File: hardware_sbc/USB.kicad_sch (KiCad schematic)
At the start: 31 parts, among them J13 USB_C_Receptacle, U1B IMX8MM, U8 NX20P3483UK, U9 PTN5110NHQZ

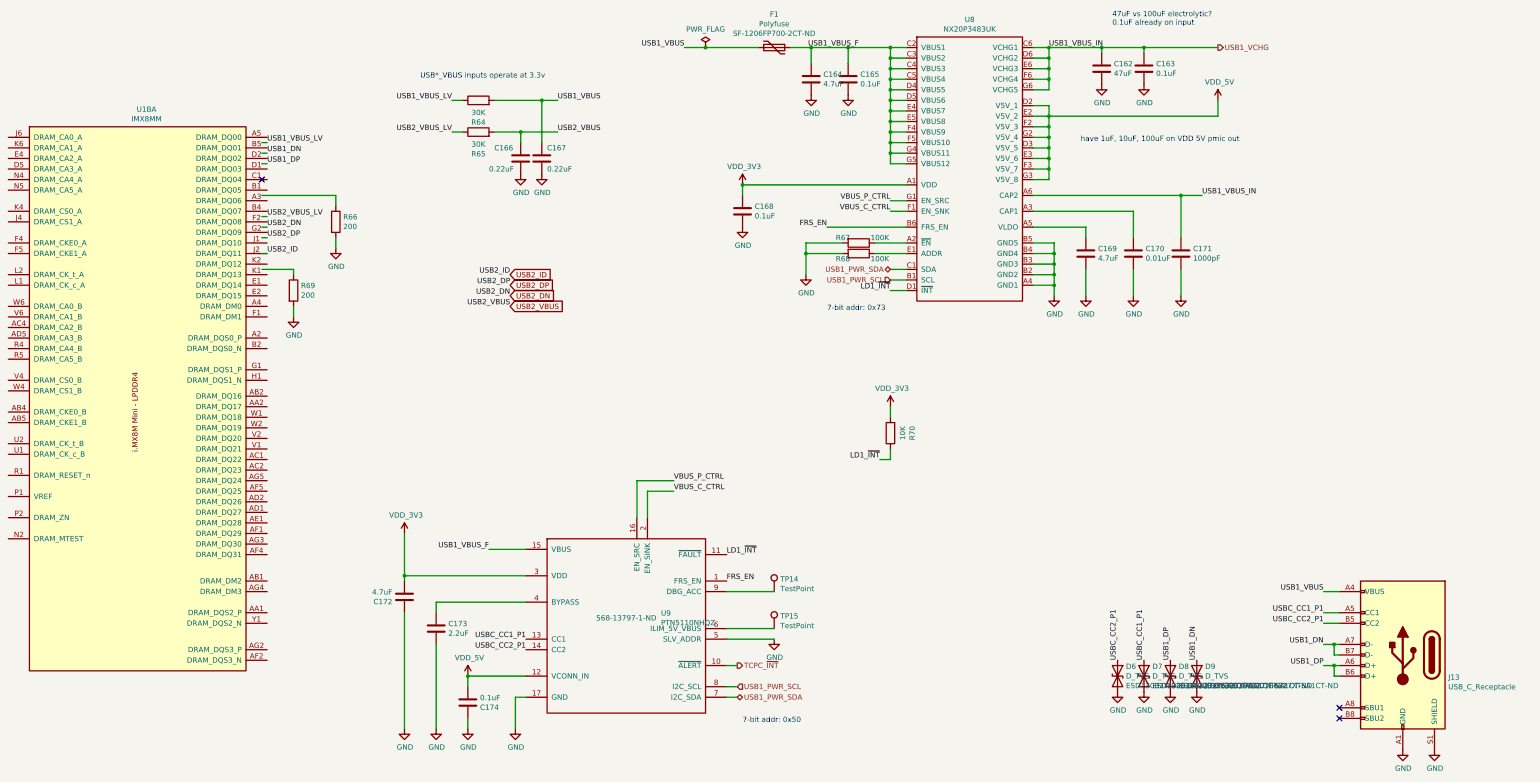
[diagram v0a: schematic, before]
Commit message: Updated production files and fixed schematic link issue.
Fixed schematic unit number issue and re-linked to PCB.
New gerbers, STEP file, schematic PDF.
Deleted old KiCAD 6 files.
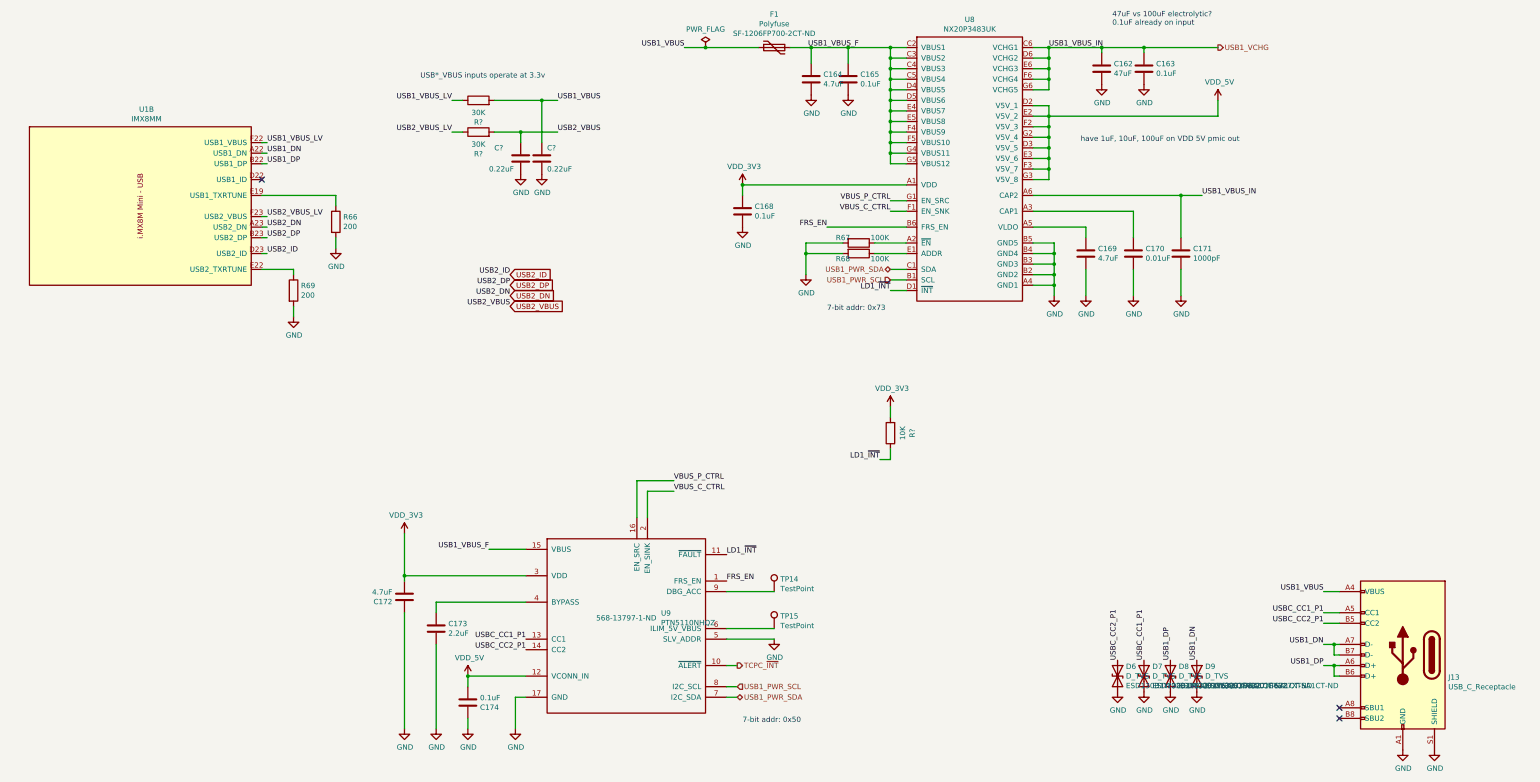
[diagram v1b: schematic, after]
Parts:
- renumbered C166 to C?, C167 to C?, R64 to R?, R65 to R?, R70 to R?, U1B to U1
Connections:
- net USB1_DN: now also U1.A22 (USB1_DN)
- net USB1_DP: now also U1.B22 (USB1_DP)
- net USB1_VBUS_LV: now also U1.F22 (USB1_VBUS)
- net USB2_DN: now also U1.A23 (USB2_DN)
- net USB2_DP: now also U1.B23 (USB2_DP)
- net USB2_ID: now also U1.D23 (USB2_ID); no longer U1.J2 (DRAM_DQ11)
- net USB2_VBUS_LV: now also U1.F23 (USB2_VBUS)
- net at R69.1: now also U1.E22 (USB2_TXRTUNE)
- net at R66.1: now also U1.E19 (USB1_TXRTUNE)
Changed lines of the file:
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@@
 	(label "USB1_DN"
 		(at 96.52 72.39 0)
+		(fields_autoplaced yes)
 		(effects
 			(font
@@
 	(label "VBUS_C_CTRL"
 		(at 246.38 86.36 180)
+		(fields_autoplaced yes)
 		(effects
 			(font
@@
 	(label "USB2_ID"
 		(at 96.52 96.52 0)
+		(fields_autoplaced yes)
 		(effects
 			(font
@@
 	(label "FRS_EN"
 		(at 207.01 175.26 0)
+		(fields_autoplaced yes)
 		(effects
 			(font
@@
 	(label "USBC_CC2_P1"
 		(at 300.99 194.31 90)
+		(fields_autoplaced yes)
 		(effects
 			(font
@@
 	(label "USBC_CC1_P1"
 		(at 350.52 182.88 180)
+		(fields_autoplaced yes)
 		(effects
 			(font
@@
 	(label "USB1_VBUS_IN"
 		(at 321.31 82.55 0)
+		(fields_autoplaced yes)
 		(effects
 			(font
@@
 	(label "VBUS_C_CTRL"
 		(at 194.31 153.67 0)
+		(fields_autoplaced yes)
 		(effects
 			(font
@@
 	(label "LD1_~{INT}"
 		(at 207.01 168.91 0)
+		(fields_autoplaced yes)
 		(effects
 			(font
@@
 	(label "USB2_VBUS_LV"
 		(at 140.97 67.31 180)
+		(fields_autoplaced yes)
 		(effects
 			(font
@@
 	(label "USBC_CC1_P1"
 		(at 158.75 189.23 180)
+		(fields_autoplaced yes)
 		(effects
 			(font
@@
 	(label "USB1_VBUS_F"
 		(at 149.86 167.64 180)
+		(fields_autoplaced yes)
 		(effects
 			(font
@@
 	(label "USB1_VBUS"
 		(at 196.85 46.99 180)
+		(fields_autoplaced yes)
 		(effects
 			(font
@@
 	(label "USB1_DN"
 		(at 320.04 194.31 90)
+		(fields_autoplaced yes)
 		(effects
 			(font
@@
 	(label "LD1_~{INT}"
 		(at 243.84 146.05 180)
+		(fields_autoplaced yes)
 		(effects
 			(font
@@
 	(label "VBUS_P_CTRL"
 		(at 194.31 151.13 0)
+		(fields_autoplaced yes)
 		(effects
 			(font
@@
 	(label "USB1_DP"
 		(at 313.69 194.31 90)
+		(fields_autoplaced yes)
 		(effects
 			(font
@@
 	(label "USB1_VBUS_IN"
 		(at 284.48 46.99 0)
+		(fields_autoplaced yes)
 		(effects
 			(font
@@
 	(label "USB1_VBUS"
 		(at 350.52 177.8 180)
+		(fields_autoplaced yes)
 		(effects
 			(font
@@
 	(label "USB1_VBUS"
 		(at 166.37 59.69 0)
+		(fields_autoplaced yes)
 		(effects
 			(font
@@
 	(label "USBC_CC2_P1"
 		(at 158.75 191.77 180)
+		(fields_autoplaced yes)
 		(effects
 			(font
@@
 	(label "USB2_DP"
 		(at 154.94 104.14 180)
+		(fields_autoplaced yes)
 		(effects
 			(font
@@
 	(label "USBC_CC1_P1"
 		(at 307.34 194.31 90)
+		(fields_autoplaced yes)
 		(effects
 			(font
@@
 	(label "USB2_ID"
 		(at 154.94 101.6 180)
+		(fields_autoplaced yes)
 		(effects
 			(font
@@
 	(label "USB1_VBUS_LV"
 		(at 96.52 69.85 0)
+		(fields_autoplaced yes)
 		(effects
 			(font
@@
 	(label "USB1_VBUS_F"
 		(at 238.76 46.99 180)
+		(fields_autoplaced yes)
 		(effects
 			(font
@@
 	(label "USBC_CC2_P1"
 		(at 350.52 185.42 180)
+		(fields_autoplaced yes)
 		(effects
 			(font
@@
 	(label "VBUS_P_CTRL"
 		(at 246.38 83.82 180)
+		(fields_autoplaced yes)
 		(effects
 			(font
@@
 	(label "USB2_VBUS"
 		(at 154.94 109.22 180)
+		(fields_autoplaced yes)
 		(effects
 			(font
@@
 	(label "USB1_DP"
 		(at 350.52 195.58 180)
+		(fields_autoplaced yes)
 		(effects
 			(font
@@
 	(label "USB2_VBUS"
 		(at 166.37 67.31 0)
+		(fields_autoplaced yes)
 		(effects
 			(font
@@
 	(label "USB1_DN"
 		(at 350.52 190.5 180)
+		(fields_autoplaced yes)
 		(effects
 			(font
@@
 	(label "LD1_~{INT}"
 		(at 246.38 105.41 180)
+		(fields_autoplaced yes)
 		(effects
 			(font
@@
 	(label "USB2_DN"
 		(at 96.52 90.17 0)
+		(fields_autoplaced yes)
 		(effects
 			(font
@@
 	(label "USB1_DP"
 		(at 96.52 74.93 0)
+		(fields_autoplaced yes)
 		(effects
 			(font
@@
 	(label "USB2_DN"
 		(at 154.94 106.68 180)
+		(fields_autoplaced yes)
 		(effects
 			(font
@@
 	(label "FRS_EN"
 		(at 231.14 90.17 180)
+		(fields_autoplaced yes)
 		(effects
 			(font
@@
 	(label "USB1_VBUS_LV"
 		(at 140.97 59.69 180)
+		(fields_autoplaced yes)
 		(effects
 			(font
@@
 	(label "USB2_DP"
 		(at 96.52 92.71 0)
+		(fields_autoplaced yes)
 		(effects
 			(font
@@
 	(label "USB2_VBUS_LV"
 		(at 96.52 87.63 0)
+		(fields_autoplaced yes)
 		(effects
 			(font
@@
 		(shape output)
 		(at 325.12 46.99 0)
+		(fields_autoplaced yes)
 		(effects
 			(font
@@
 		(shape bidirectional)
 		(at 246.38 100.33 180)
+		(fields_autoplaced yes)
 		(effects
 			(font
@@
 		(shape input)
 		(at 246.38 102.87 180)
+		(fields_autoplaced yes)
 		(effects
 			(font
@@
 		(shape bidirectional)
 		(at 209.55 203.2 0)
+		(fields_autoplaced yes)
 		(effects
 			(font
@@
 		(shape input)
 		(at 209.55 200.66 0)
+		(fields_autoplaced yes)
 		(effects
 			(font
@@
 		(shape output)
 		(at 209.55 195.58 0)
+		(fields_autoplaced yes)
 		(effects
 			(font
@@
 		(lib_id "mxenc:MIMX8MM6DVTLZAA")
 		(at 66.04 134.62 0)
-		(unit 1)
+		(unit 2)
 		(exclude_from_sim no)
 		(in_bom yes)
 		(on_board yes)
 		(dnp no)
-		(property "Reference" "U1B"
+		(property "Reference" "U1"
 			(at 67.5132 61.849 0)
 			(effects
@@
 			(project "kimchi_micro"
 				(path "/394ea9d6-84ac-414f-b42c-59edf258c746/00000000-0000-0000-0000-00005d6742b7"
-					(reference "U1B")
-					(unit 1)
+					(reference "U1")
+					(unit 2)
 				)
 			)
@@
 		(on_board yes)
 		(dnp no)
-		(property "Reference" "R64"
+		(property "Reference" "R?"
 			(at 147.32 64.9478 90)
 			(effects
@@
 		(on_board yes)
 		(dnp no)
-		(property "Reference" "R65"
+		(property "Reference" "R?"
 			(at 147.32 72.5678 90)
 			(effects
@@
 		(on_board yes)
 		(dnp no)
-		(property "Reference" "C166"
+		(property "Reference" "C?"
 			(at 151.13 71.12 0)
 			(effects
@@
 		(on_board yes)
 		(dnp no)
-		(property "Reference" "C167"
+		(property "Reference" "C?"
 			(at 163.83 71.12 0)
 			(effects
@@
 		(on_board yes)
 		(dnp no)
-		(property "Reference" "R70"
+		(property "Reference" "R?"
 			(at 251.6378 139.7 90)
 			(effects
